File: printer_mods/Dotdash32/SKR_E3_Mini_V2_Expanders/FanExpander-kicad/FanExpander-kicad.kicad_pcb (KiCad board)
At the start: 2 copper layers, 52 parts, among them J1 FAN1_IN, J10 FAN2, J11 V_SELECT3, J12 V_SELECT4, J13 FAN3, J14 FAN4, J15 V_SELECT5, J16 V_SELECT6, J17 FAN5, J18 FAN6, J2 HV_IN, J3 EXP1_IN, J4 TH2, J5 3V3_IN, J6 V_SELECT1, J7 V_SELECT2, J8 TH2, J9 FAN1, Q1 IRLML6344, Q2 IRLML6344, Q3 IRLML6344, Q4 IRLML6344, Q5 IRLML6344

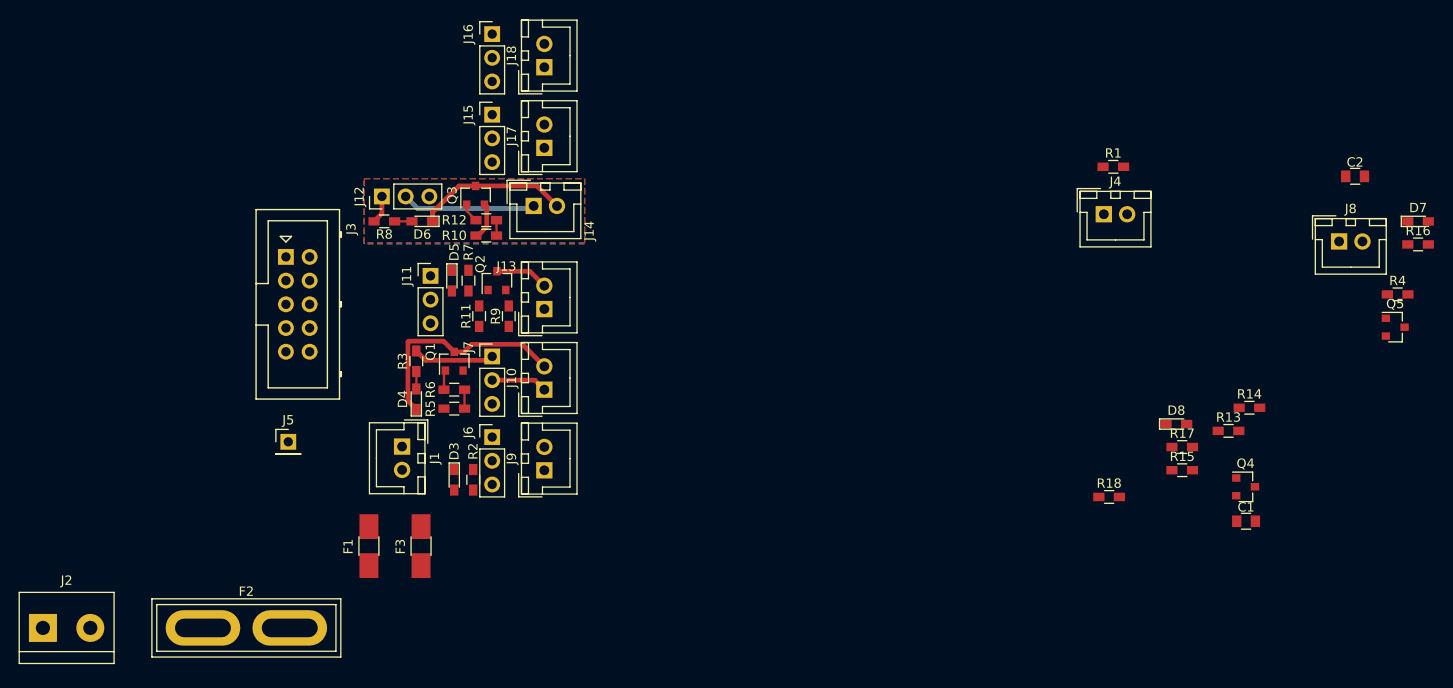
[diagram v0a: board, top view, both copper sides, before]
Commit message: feat: no ADC in EXP1, add more fans!!!
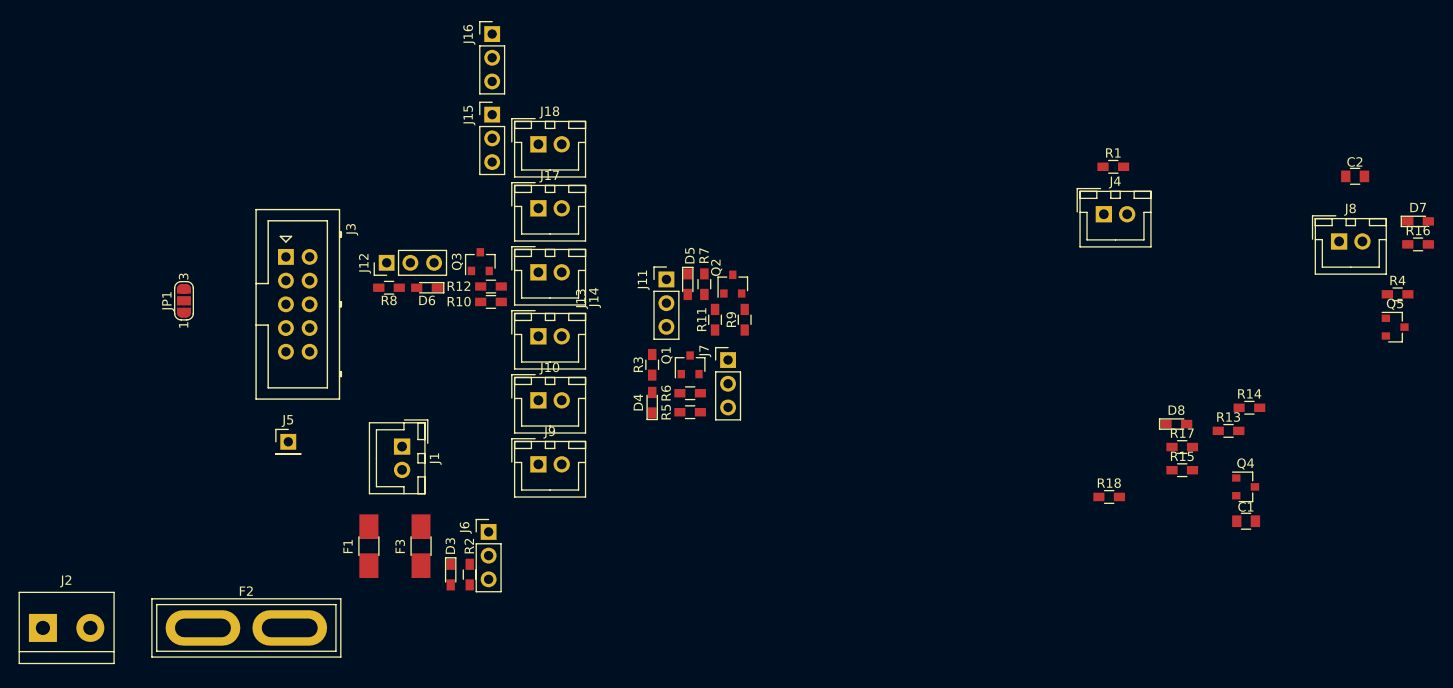
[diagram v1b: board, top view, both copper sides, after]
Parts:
- added JP1: FAN_SEL, Jumper:SolderJumper-3_P1.3mm_Open_RoundedPad1.0x1.5mm_NumberLabels, F.Cu at (32.5, 50.4)
- moved J7 25.3 mm to (90.8, 56.8)
- moved D4 25.3 mm to (82.7, 61.3)
- moved R3 25.3 mm to (82.7, 57.3)
- moved R7 25.3 mm to (88.3, 48.6)
- moved D5 25.3 mm to (86.5, 48.6)
- moved J11 25.3 mm to (84.2, 48.1)
- moved Q1 25.3 mm to (86.7, 57.3)
- moved Q2 25.3 mm to (91.3, 48.6)
- moved R11 25.3 mm to (89.4, 52.5)
- moved R5 25.3 mm to (86.7, 62.4)
- moved R6 25.3 mm to (86.7, 60.3)
- moved R9 25.3 mm to (92.6, 52.5)
- moved D3 10.2 mm to (61.1, 79.8)
- moved J6 10.2 mm to (65.2, 75.2)
- moved R2 10.2 mm to (63.1, 79.8)
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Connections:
- F1 pad 2: /toFuse24V -> Net-(F1-Pad2)
- F3 pad 2: /toFuse5V -> Net-(F3-Pad2)
- J1 pad 1: /toFuse24V -> /24V_unFused
- J15 pad 2: /F5V -> Net-(J15-Pad2)
- J16 pad 1: +5V -> Net-(J16-Pad1)
- J16 pad 2: /F6V -> Net-(J16-Pad2)
- J16 pad 3: +24V -> Net-(J16-Pad3)
- J17 pad 1: /F5V -> Net-(J17-Pad1)
- J3 pad 10: /toFuse5V -> /5V_unFused
- J3 pad 2: /FAN4 -> /FAN6
- J3 pad 3: /TH2 -> /FAN3
- J3 pad 5: /TH3 -> /FAN4
- J3 pad 6: /FAN5 -> /FAN7
- J3 pad 7: /FAN3 -> /FAN5
- J3 pad 8: /FAN6 -> Net-(J3-Pad8)
- J6 pad 1: +5V -> Net-(J6-Pad1)
- J6 pad 2: /F1V -> Net-(J6-Pad2)
- J6 pad 3: +24V -> Net-(J6-Pad3)
- R10 pad 1: /FAN4 -> GND
- R10 pad 2: GND -> /FAN4
- R13 pad 2: +5V -> Net-(R13-Pad2)
- R3 pad 2: +5V -> /LED_Drive
- R7 pad 2: +5V -> /LED_Drive
- R8 pad 2: +5V -> /LED_Drive
- R9 pad 1: /FAN3 -> GND
- R9 pad 2: GND -> /FAN3
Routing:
- net /FAN2_Drive: track 24.0 -> 0.00 mm
- net /FAN4_Drive: track 16.4 -> 0.00 mm
- net /F4V: track 14.4 -> 0.00 mm
- net +5V: track 11.7 -> 0.00 mm
- net /F2V: track 6.01 -> 0.00 mm
- net /FAN3_Drive: track 5.72 -> 0.00 mm
- net GND: track 4.02 -> 0.00 mm
- net Net-(Q1-Pad1): track 2.11 -> 0.00 mm
- net Net-(Q3-Pad1): track 2.08 -> 0.00 mm
- net /FAN2: track 2.03 -> 0.00 mm
- net Net-(D6-Pad2): track 1.86 -> 0.00 mm
- net Net-(D4-Pad2): track 1.86 -> 0.00 mm
- net /FAN4: track 1.65 -> 0.00 mm
- removed copper zone on B.Cu, net GND
- removed copper zone on F.Cu, net GND

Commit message: feat: beefy expander sch cleaned, initial layout
schematic looks good, but the layout needs work.
RN, it covers too much, so needs to have the EXP header stick out
a lot more than it already is, probably make the whole thing longer
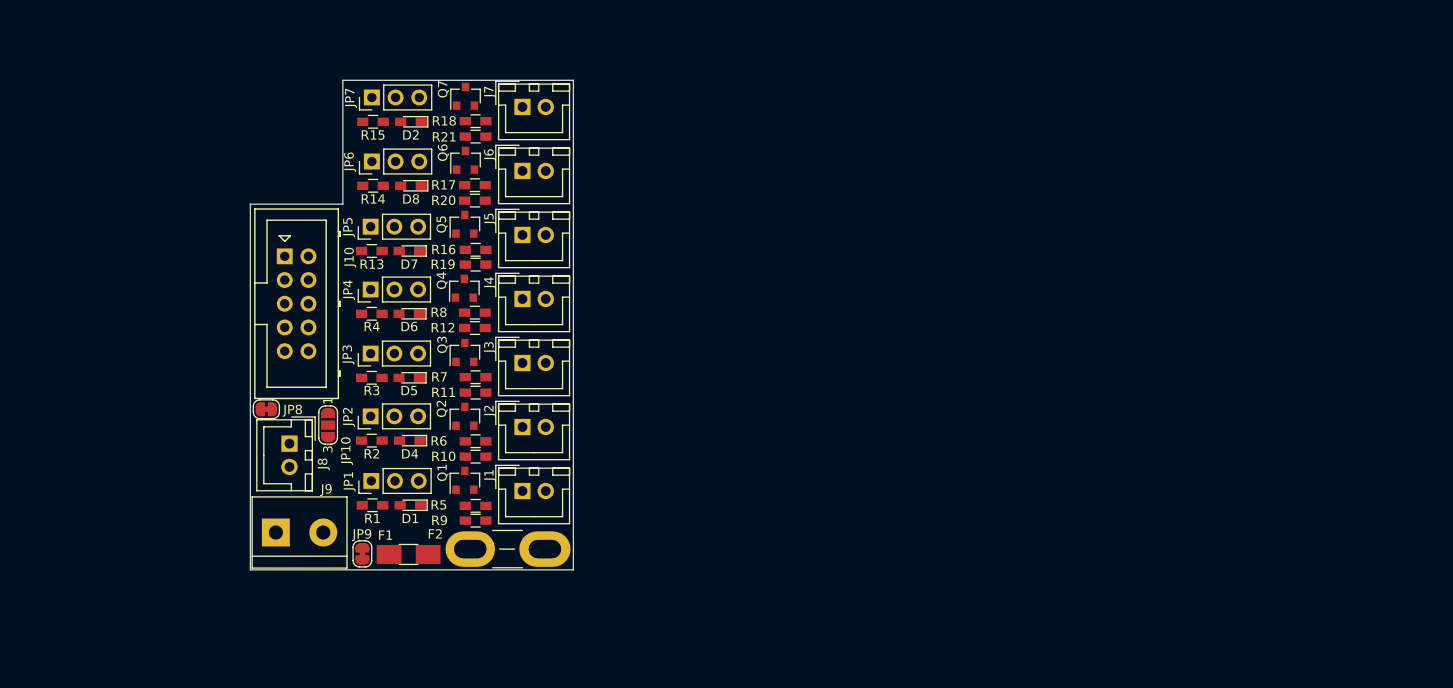
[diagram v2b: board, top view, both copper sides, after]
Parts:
- removed C1, C2: 10uF, Capacitors_SMD:C_0805
- removed D3: LED, LEDs:LED_0603_HandSoldering
- removed F3: Polyfuse-1A, Fuse_Holders_and_Fuses:Fuse_SMD1206_HandSoldering
- removed the J2 at (17.4, 85.5)
- removed the J3 at (43.4, 45.7)
- removed the J4 at (131.1, 41.1)
- removed the J5 at (43.7, 65.5)
- removed the J6 at (65.2, 75.2)
- removed the J8 at (156.3, 44.1)
- removed the R2 at (63.1, 79.8)
- removed the R4 at (162.5, 49.7)
- added D1: LED, LEDs:LED_0603_HandSoldering, F.Cu at (56.8, 72.3)
- added D2: LED, LEDs:LED_0603_HandSoldering, F.Cu at (56.8, 31.2)
- added J1: FAN1, Connectors_JST:JST_XH_B02B-XH-A_02x2.50mm_Straight, F.Cu at (68.8, 70.8)
- added J10: EXP1_IN, Connectors_Multicomp:Multicomp_MC9A12-1034_2x05x2.54mm_Straight, F.Cu at (43.3, 45.7)
- added J7: FAN7, Connectors_JST:JST_XH_B02B-XH-A_02x2.50mm_Straight, F.Cu at (68.8, 29.7)
- added JP10: FAN_SEL, Jumper:SolderJumper-3_P1.3mm_Open_RoundedPad1.0x1.5mm_NumberLabels, F.Cu at (48.0, 63.7)
- added JP7: V_SELECT7, Pin_Headers:Pin_Header_Straight_1x03_Pitch2.54mm, F.Cu at (52.6, 28.6)
- added JP8: 5V_EXP_CONN, Jumper:SolderJumper-2_P1.3mm_Bridged_RoundedPad1.0x1.5mm, F.Cu at (41.3, 62.0)
- added JP9: LED_ENABLE, Jumper:SolderJumper-2_P1.3mm_Bridged_RoundedPad1.0x1.5mm, F.Cu at (51.6, 77.5)
- added Q1: IRLML6344, TO_SOT_Packages_SMD:SOT-23, F.Cu at (62.6, 69.7)
- added Q7: IRLML6344, TO_SOT_Packages_SMD:SOT-23, F.Cu at (62.7, 28.5)
- added R18: 100R, Resistors_SMD:R_0603_HandSoldering, F.Cu at (63.8, 31.2)
- added R19: 100k, Resistors_SMD:R_0603_HandSoldering, F.Cu at (63.8, 46.5)
- added R21: 100k, Resistors_SMD:R_0603_HandSoldering, F.Cu at (63.8, 32.8)
- added R5: 100R, Resistors_SMD:R_0603_HandSoldering, F.Cu at (63.8, 72.4)
- added R9: 100k, Resistors_SMD:R_0603_HandSoldering, F.Cu at (63.8, 74.0)
- F1: value Polyfuse-2A -> Polyfuse-1A
- F2: footprint Fuse_Holders_and_Fuses:BladeFuse-CarType -> Fuse_Holders_and_Fuses:BladeFuse-Mini
- J8: renamed from J1; value FAN1_IN -> 5V_In
- J9: value FAN1 -> HV_IN; footprint Connectors_JST:JST_XH_B02B-XH-A_02x2.50mm_Straight -> Connectors_Terminal_Blocks:TerminalBlock_bornier-2_P5.08mm
- JP1: value FAN_SEL -> V_SELECT1; footprint Jumper:SolderJumper-3_P1.3mm_Open_RoundedPad1.0x1.5mm_NumberLabels -> Pin_Headers:Pin_Header_Straight_1x03_Pitch2.54mm
- R1: value 4.7k -> 560R
- R15: value 100k -> 560R
- moved D7 108.1 mm to (56.7, 45.1), turned to 180 degrees
- moved Q6 101.2 mm to (62.7, 35.4), turned to 90 degrees
- moved R20 101.2 mm to (63.7, 39.7), turned to 180 degrees
- moved R14 96.9 mm to (52.8, 38.1), turned to 180 degrees
- moved R15 94.4 mm to (52.8, 31.2), turned to 180 degrees
- moved R13 93.8 mm to (52.6, 45.1), turned to 180 degrees
- moved Q5 88.2 mm to (62.6, 42.2), turned to 90 degrees
- moved R1 87.3 mm to (52.7, 72.3), turned to 180 degrees
- moved D8 85.9 mm to (56.8, 38.1), turned to 180 degrees
- moved R16 78.6 mm to (63.8, 45.0)
- moved R17 75.7 mm to (63.7, 38.0)
- moved JP2 38.8 mm to (52.5, 62.8), turned to 90 degrees
- moved F2 37.6 mm to (71.2, 77.0), turned to 180 degrees
- moved R3 37.0 mm to (52.6, 58.7), turned to 180 degrees
- moved JP3 32.7 mm to (52.5, 56.1), turned to 90 degrees
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- renumbered J10 to J2, J13 to J3, J14 to J4, J17 to J5, J18 to J6, J7 to JP2, J11 to JP3, J12 to JP4, J15 to JP5, J16 to JP6, Q1 to Q2, Q2 to Q3, Q3 to Q4, Q4 to Q5, Q5 to Q6, R5 to R10, R9 to R11, R10 to R12, R17 to R16, R18 to R17, R3 to R2, R16 to R20, R7 to R3, R8 to R4, R11 to R7, R12 to R8
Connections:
- net /FAN2_Drive renamed /FAN2_Dr
- net /FAN3_Drive renamed /FAN3_Dr
- net /FAN4_Drive renamed /FAN4_Dr
- net /FAN5_Drive renamed /FAN5_Dr
- net /FAN6_Drive renamed /FAN6_Dr
- F1 pad 1: +24V -> +5V
- F1 pad 2: Net-(F1-Pad2) -> /5V_unFused
- F2 pad 2: /toFuseHV -> /24V_unFused
- J5 pad 1: Net-(J17-Pad1) -> /F5V
- J8 pad 1: /24V_unFused -> /5V_unFused
- J8 pad 2: /FAN1_Drive -> GND
- J9 pad 1: /F1V -> /24V_unFused
- J9 pad 2: /FAN1_Drive -> GND
- JP1 pad 1: Net-(J3-Pad8) -> +5V
- JP1 pad 2: /FAN8 -> /F1V
- JP1 pad 3: Net-(J3-Pad4) -> +24V
- JP5 pad 2: Net-(J15-Pad2) -> /F5V
- JP6 pad 1: Net-(J16-Pad1) -> +5V
- JP6 pad 2: Net-(J16-Pad2) -> /F6V
- JP6 pad 3: Net-(J16-Pad3) -> +24V
- R1 pad 1: +3V3 -> Net-(D1-Pad2)
- R1 pad 2: /TH2 -> /LED_Drive
- R13 pad 2: Net-(R13-Pad2) -> /LED_Drive
- R14 pad 2: +5V -> /LED_Drive
- R15 pad 1: /FAN5 -> Net-(D2-Pad2)
- R15 pad 2: GND -> /LED_Drive
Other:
- board outline added: 34.6 x 52.5 mm

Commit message: test: using 1xXX pins for breakaways?
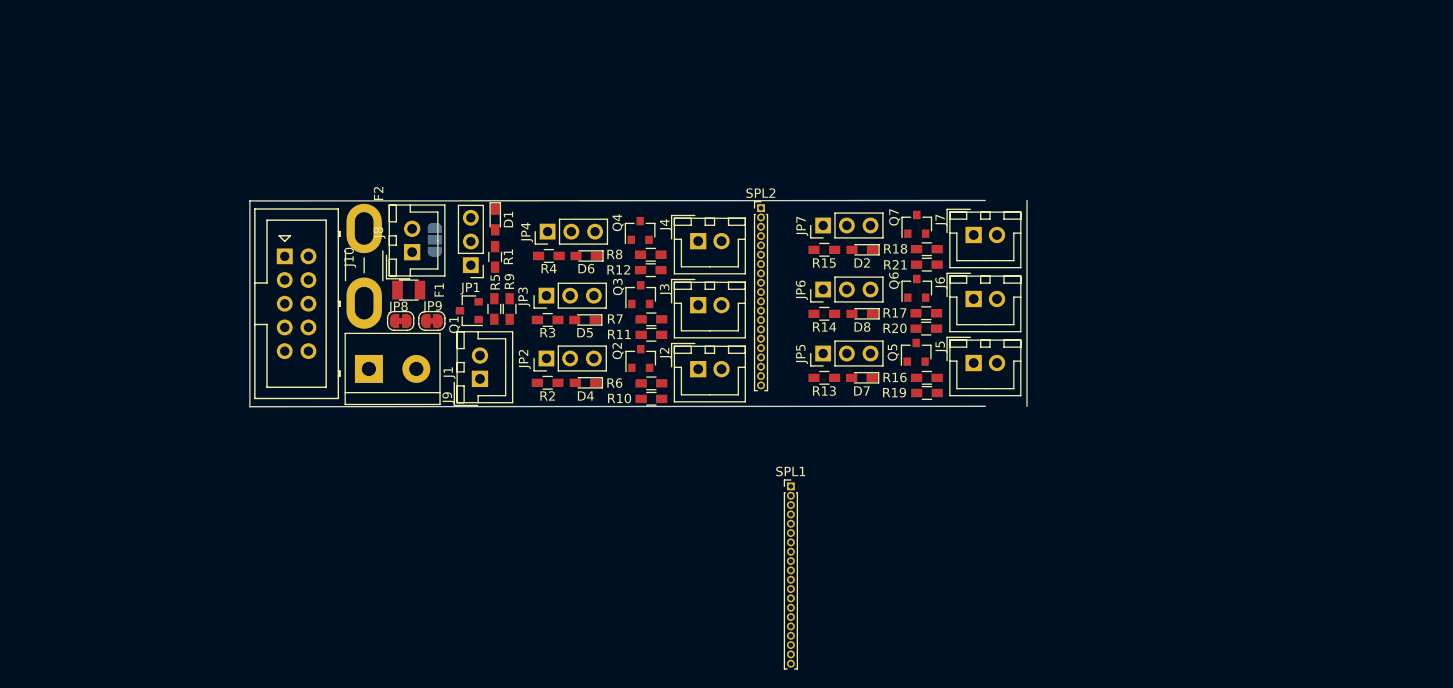
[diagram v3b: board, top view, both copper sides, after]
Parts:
- added SPL1: Breakaway, Pin_Headers:Pin_Header_Straight_1x20_Pitch1.00mm, F.Cu at (97.5, 70.3)
- added SPL2: Breakaway, Pin_Headers:Pin_Header_Straight_1x20_Pitch1.00mm, F.Cu at (94.3, 40.5)
- F1: footprint Fuse_Holders_and_Fuses:Fuse_SMD1206_HandSoldering -> Fuse_Holders_and_Fuses:Fuse_SMD1206_Reflow
- JP10: moved to B.Cu
- moved D7 50.3 mm to (105.1, 58.7)
- moved R13 50.3 mm to (101.1, 58.7)
- moved JP5 50.3 mm to (101.0, 56.1)
- moved R19 50.3 mm to (112.1, 60.3)
- moved Q5 50.3 mm to (111.0, 55.9)
- moved R16 50.3 mm to (112.1, 58.7)
- moved R18 50.3 mm to (112.1, 44.9)
- moved R21 50.3 mm to (112.1, 46.5)
- moved J5 50.3 mm to (117.1, 57.1)
- moved J6 50.3 mm to (117.1, 50.2)
- moved J7 50.3 mm to (117.1, 43.4)
- moved R14 50.3 mm to (101.1, 51.8)
- moved R15 50.3 mm to (101.1, 45.0)
- moved R17 50.3 mm to (112.0, 51.8)
- moved R20 50.3 mm to (112.0, 53.4)
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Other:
- board size 34.6 x 52.5 mm -> 83.3 x 22.1 mm
